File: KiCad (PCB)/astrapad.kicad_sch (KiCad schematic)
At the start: 34 parts, among them J1 OLED_DISPLAY, SW1 SW_Push, SW13 RotaryEncoder_Switch, SW2 SW_Push, SW3 SW_Push, SW5 SW_Push, SW6 SW_Push, SW7 SW_Push, SW8 SW_Push, U1 XIAO-RP2040-DIP

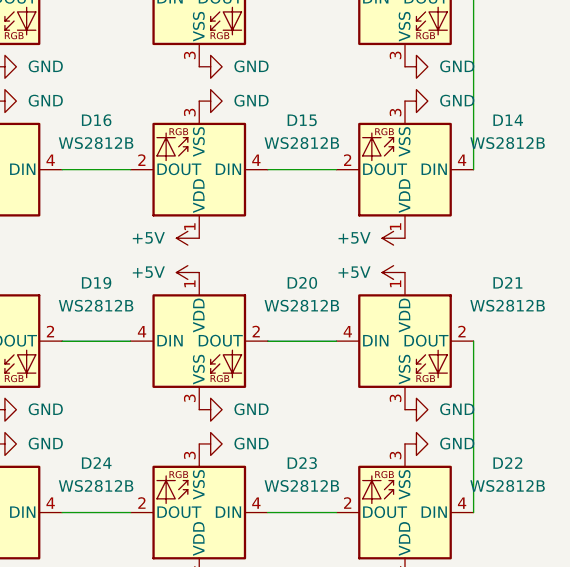
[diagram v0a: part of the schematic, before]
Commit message: Resized PCB to fit 100mmx100mm limit Turns out the PCB has a max size of 100mmx100mm, mine was 106x59. I resized it though so we good now
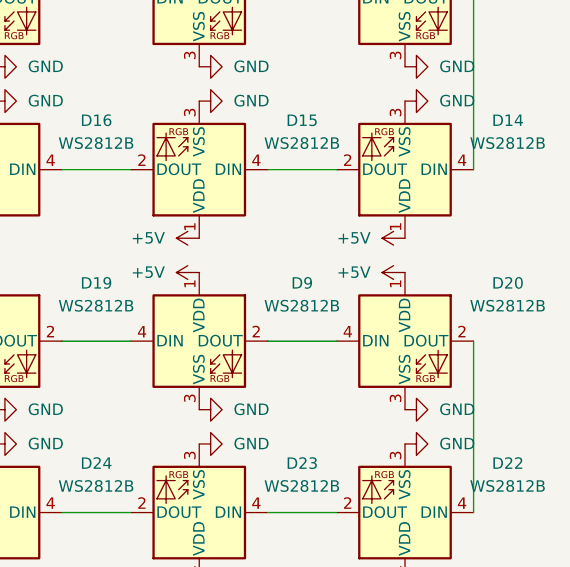
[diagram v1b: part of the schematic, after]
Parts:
- removed D21: WS2812B, LED_SMD:LED_SK6812MINI_PLCC4_3.5x3.5mm_P1.75mm, symbol LED:WS2812B
- added D9: WS2812B, LED_SMD:LED_SK6812MINI_PLCC4_3.5x3.5mm_P1.75mm, symbol LED:WS2812B
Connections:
- net +5V: now also D9.1 (VDD)
- net GND: now also D9.3 (VSS)
- net at D22.4 (DIN): now also D20.2 (DOUT)
- net at D19.2 (DOUT): now also D9.4 (DIN); no longer D20.4 (DIN)
- new net: D20.4 (DIN), D9.2 (DOUT)
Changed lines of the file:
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@@
 	(wire
 		(pts
+			(xy 261.62 170.18) (xy 269.24 170.18)
+		)
+		(stroke
+			(width 0)
+			(type default)
+		)
+	)
+	(wire
+		(pts
 			(xy 102.87 100.33) (xy 88.9 100.33)
 		)
@@
 	(wire
 		(pts
-			(xy 261.62 170.18) (xy 269.24 170.18)
-		)
-		(stroke
-			(width 0)
-			(type default)
-		)
-	)
-	(wire
-		(pts
 			(xy 215.9 189.23) (xy 223.52 189.23)
 		)
@@
 	)
 	(symbol
+		(lib_id "LED:WS2812B")
+		(at 254 170.18 0)
+		(unit 1)
+		(exclude_from_sim no)
+		(in_bom yes)
+		(on_board yes)
+		(dnp no)
+		(fields_autoplaced yes)
+		(property "Reference" "D9"
+			(at 265.43 163.7598 0)
+			(effects
+				(font
+					(size 1.27 1.27)
+				)
+			)
+		)
+		(property "Value" "WS2812B"
+			(at 265.43 166.2998 0)
+			(effects
+				(font
+					(size 1.27 1.27)
+				)
+			)
+		)
+		(property "Footprint" "LED_SMD:LED_SK6812MINI_PLCC4_3.5x3.5mm_P1.75mm"
+			(at 255.27 177.8 0)
+			(effects
+				(font
+					(size 1.27 1.27)
+				)
+				(justify left top)
+				(hide yes)
+			)
+		)
+		(property "Datasheet" "https://cdn-shop.adafruit.com/datasheets/WS2812B.pdf"
+			(at 256.54 179.705 0)
+			(effects
+				(font
+					(size 1.27 1.27)
+				)
+				(justify left top)
+				(hide yes)
+			)
+		)
+		(property "Description" "RGB LED with integrated controller"
+			(at 254 170.18 0)
+			(effects
+				(font
+					(size 1.27 1.27)
+				)
+				(hide yes)
+			)
+		)
+		(pin "1"
+		)
+		(pin "4"
+		)
+		(pin "3"
+		)
+		(pin "2"
+		)
+		(instances
+			(project "astrapad"
+				(path "/5abc847e-aba8-4487-9719-b82ae41842b5"
+					(reference "D9")
+					(unit 1)
+				)
+			)
+		)
+	)
+	(symbol
 		(lib_id "Connector:Conn_01x04_Pin")
 		(at 107.95 95.25 270)
@@
 	)
 	(symbol
-		(lib_id "LED:WS2812B")
-		(at 276.86 170.18 0)
-		(unit 1)
-		(exclude_from_sim no)
-		(in_bom yes)
-		(on_board yes)
-		(dnp no)
-		(fields_autoplaced yes)
-		(property "Reference" "D21"
-			(at 288.29 163.7598 0)
-			(effects
-				(font
-					(size 1.27 1.27)
-				)
-			)
-		)
-		(property "Value" "WS2812B"
-			(at 288.29 166.2998 0)
-			(effects
-				(font
-					(size 1.27 1.27)
-				)
-			)
-		)
-		(property "Footprint" "LED_SMD:LED_SK6812MINI_PLCC4_3.5x3.5mm_P1.75mm"
-			(at 278.13 177.8 0)
-			(effects
-				(font
-					(size 1.27 1.27)
-				)
-				(justify left top)
-				(hide yes)
-			)
-		)
-		(property "Datasheet" "https://cdn-shop.adafruit.com/datasheets/WS2812B.pdf"
-			(at 279.4 179.705 0)
-			(effects
-				(font
-					(size 1.27 1.27)
-				)
-				(justify left top)
-				(hide yes)
-			)
-		)
-		(property "Description" "RGB LED with integrated controller"
-			(at 276.86 170.18 0)
-			(effects
-				(font
-					(size 1.27 1.27)
-				)
-				(hide yes)
-			)
-		)
-		(pin "1"
-		)
-		(pin "4"
-		)
-		(pin "3"
-		)
-		(pin "2"
-		)
-		(instances
-			(project ""
-				(path "/5abc847e-aba8-4487-9719-b82ae41842b5"
-					(reference "D21")
-					(unit 1)
-				)
-			)
-		)
-	)
-	(symbol
 		(lib_id "Diode:1N4148WT")
 		(at 120.65 104.14 90)
@@
 	)
 	(symbol
-		(lib_id "LED:WS2812B")
-		(at 254 170.18 0)
-		(unit 1)
-		(exclude_from_sim no)
-		(in_bom yes)
-		(on_board yes)
-		(dnp no)
-		(fields_autoplaced yes)
-		(property "Reference" "D20"
-			(at 265.43 163.7598 0)
-			(effects
-				(font
-					(size 1.27 1.27)
-				)
-			)
-		)
-		(property "Value" "WS2812B"
-			(at 265.43 166.2998 0)
-			(effects
-				(font
-					(size 1.27 1.27)
-				)
-			)
-		)
-		(property "Footprint" "LED_SMD:LED_SK6812MINI_PLCC4_3.5x3.5mm_P1.75mm"
-			(at 255.27 177.8 0)
-			(effects
-				(font
-					(size 1.27 1.27)
-				)
-				(justify left top)
-				(hide yes)
-			)
-		)
-		(property "Datasheet" "https://cdn-shop.adafruit.com/datasheets/WS2812B.pdf"
-			(at 256.54 179.705 0)
-			(effects
-				(font
-					(size 1.27 1.27)
-				)
-				(justify left top)
-				(hide yes)
-			)
-		)
-		(property "Description" "RGB LED with integrated controller"
-			(at 254 170.18 0)
-			(effects
-				(font
-					(size 1.27 1.27)
-				)
-				(hide yes)
-			)
-		)
-		(pin "1"
-		)
-		(pin "4"
-		)
-		(pin "3"
-		)
-		(pin "2"
-		)
-		(instances
-			(project ""
-				(path "/5abc847e-aba8-4487-9719-b82ae41842b5"
-					(reference "D20")
-					(unit 1)
-				)
-			)
-		)
-	)
-	(symbol
 		(lib_id "Switch:SW_Push")
 		(at 128.27 135.89 0)
@@
 					(unit 1)
 				)
+			)
+		)
+	)
+	(symbol
+		(lib_id "LED:WS2812B")
+		(at 276.86 170.18 0)
+		(unit 1)
+		(exclude_from_sim no)
+		(in_bom yes)
+		(on_board yes)
+		(dnp no)
+		(fields_autoplaced yes)
+		(property "Reference" "D20"
+			(at 288.29 163.7598 0)
+			(effects
+				(font
+					(size 1.27 1.27)
+				)
+			)
+		)
+		(property "Value" "WS2812B"
+			(at 288.29 166.2998 0)
+			(effects
+				(font
+					(size 1.27 1.27)
+				)
+			)
+		)
+		(property "Footprint" "LED_SMD:LED_SK6812MINI_PLCC4_3.5x3.5mm_P1.75mm"
+			(at 278.13 177.8 0)
+			(effects
+				(font
+					(size 1.27 1.27)
+				)
+				(justify left top)
+				(hide yes)
+			)
+		)
+		(property "Datasheet" "https://cdn-shop.adafruit.com/datasheets/WS2812B.pdf"
+			(at 279.4 179.705 0)
+			(effects
+				(font
+					(size 1.27 1.27)
+				)
+				(justify left top)
+				(hide yes)
+			)
+		)
+		(property "Description" "RGB LED with integrated controller"
+			(at 276.86 170.18 0)
+			(effects
+				(font
+					(size 1.27 1.27)
+				)
+				(hide yes)
+			)
+		)
+		(pin "1"
+		)
+		(pin "4"
+		)
+		(pin "3"
+		)
+		(pin "2"
+		)
+		(instances
+			(project "astrapad"
+				(path "/5abc847e-aba8-4487-9719-b82ae41842b5"
+					(reference "D20")
+					(unit 1)
+				)
